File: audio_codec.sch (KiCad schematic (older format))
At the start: 11 parts

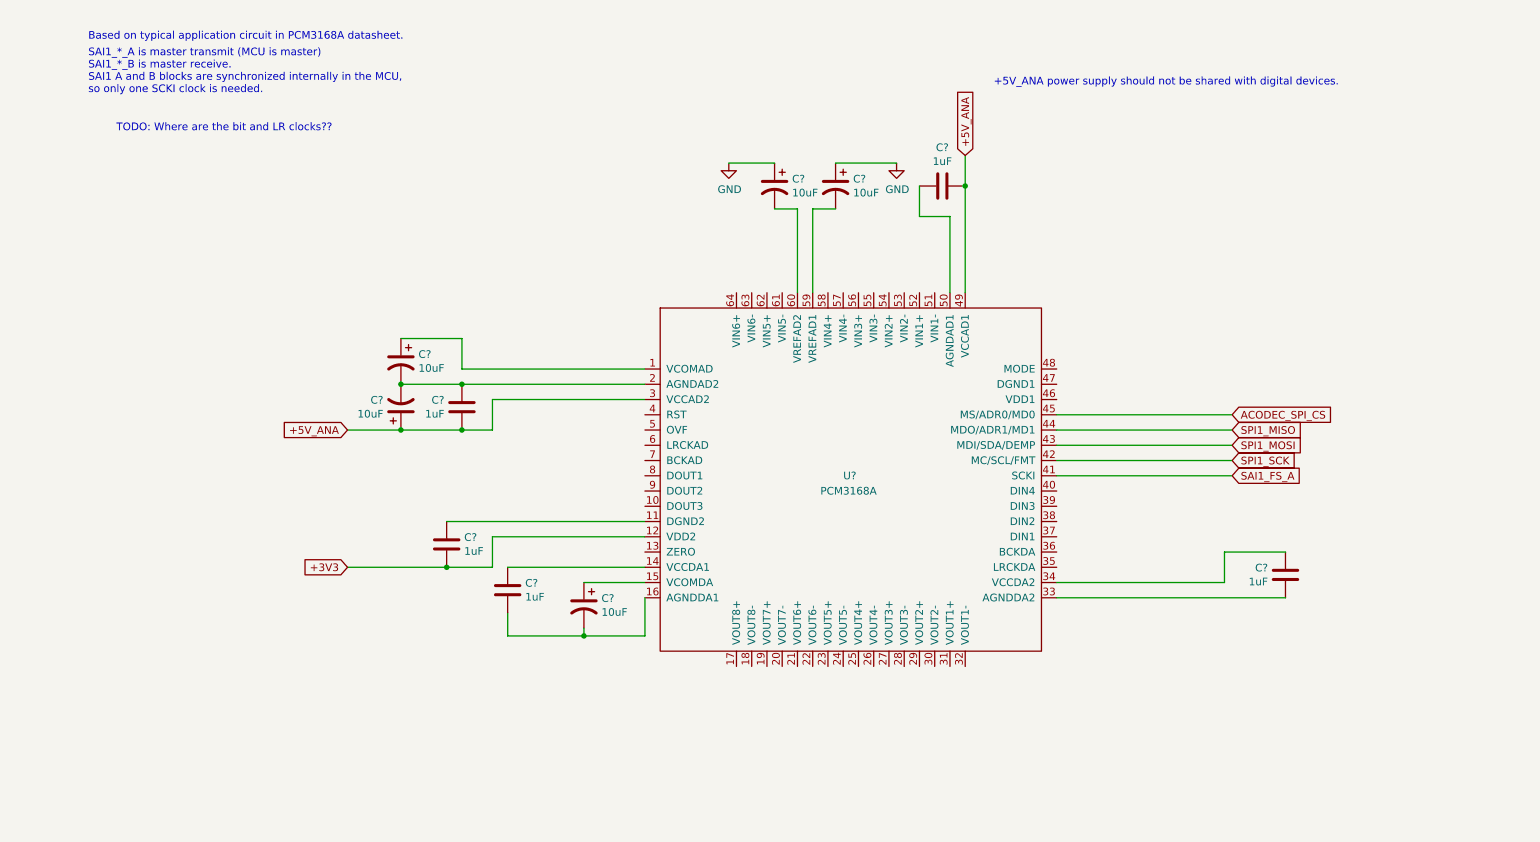
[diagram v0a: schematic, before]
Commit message: Finished digital part of CODEC
Needed to add SAI2 to get enough pins.
We could have multiplexed all 8 channels on one pin but the SR is limited to
48KHz. I wanted to see how it works with 2 data lines per direction. Then
maximum SR is 96KHz, which we probably won't use but at least its not at the
limit.
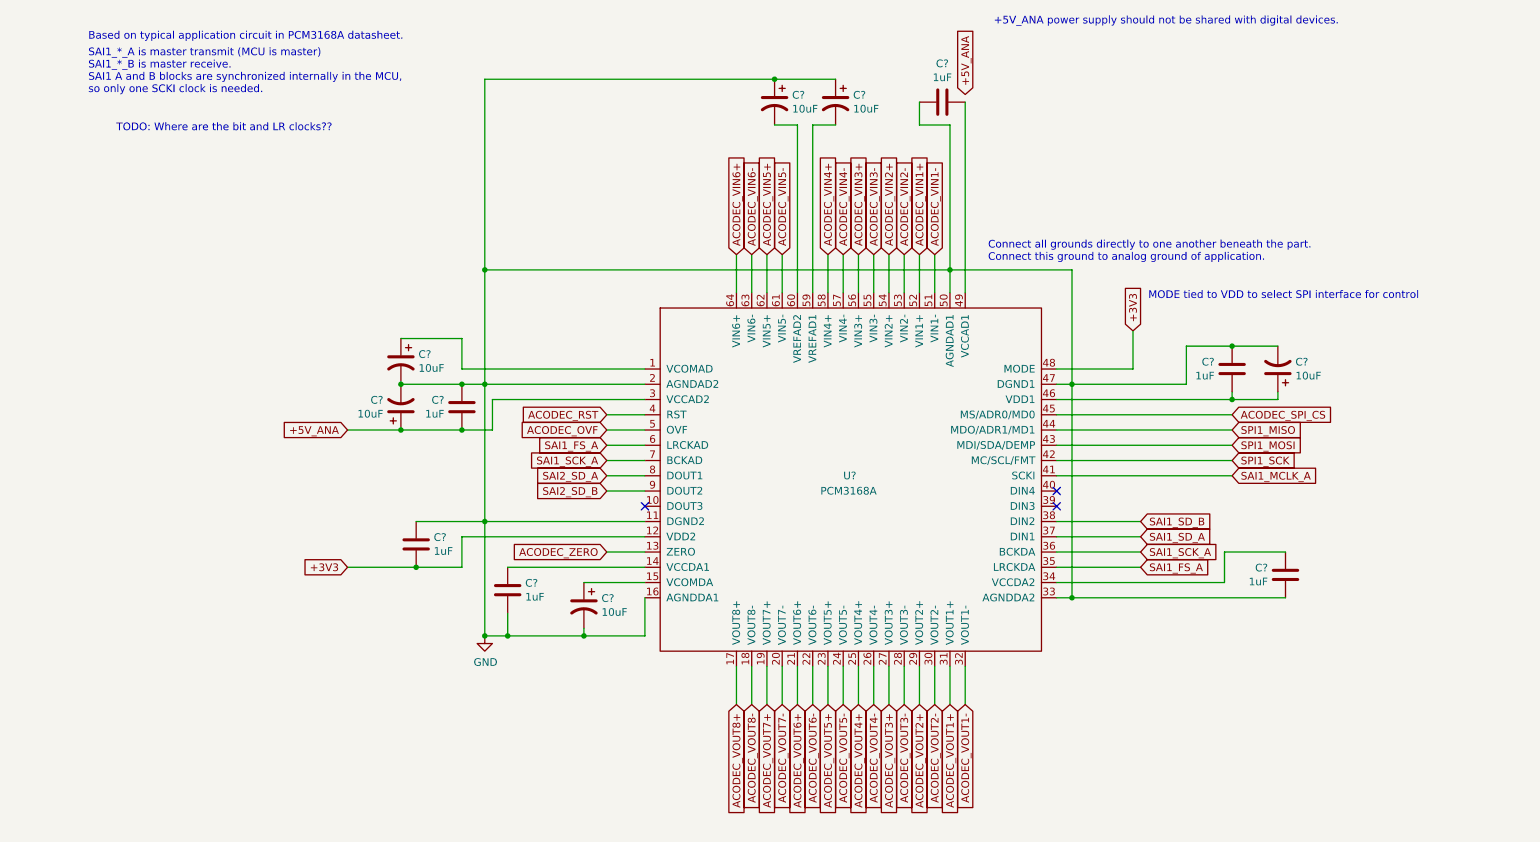
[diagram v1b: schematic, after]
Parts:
- added C?: 1uF, symbol Device:C
- added C?: 10uF, symbol Device:CP1
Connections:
- net +3V3: now also U?.48 (MODE)
- net +5V_ANA: no longer C?.1, U?.49 (VCCAD1)
- net GND: now also C?.1, C?.1, C?.2, C?.2, C?.2, C?.2, C?.2, C?.2, U?.11 (DGND2), U?.16 (AGNDDA1), U?.2 (AGNDAD2), U?.33 (AGNDDA2), U?.47 (DGND1), U?.50 (AGNDAD1), C?.1, C?.2
- net SAI1_FS_A: now also U?.35 (LRCKDA), U?.6 (LRCKAD); no longer U?.41 (SCKI)
- net ACODEC_ZERO: now reaches U?.13 (ZERO)
- net ACODEC_VOUT8+: now reaches U?.17 (VOUT8+)
- net ACODEC_VOUT8-: now reaches U?.18 (VOUT8-)
- net ACODEC_VOUT7+: now reaches U?.19 (VOUT7+)
- net ACODEC_VOUT7-: now reaches U?.20 (VOUT7-)
- net ACODEC_VOUT6+: now reaches U?.21 (VOUT6+)
- net ACODEC_VOUT6-: now reaches U?.22 (VOUT6-)
- net ACODEC_VOUT5+: now reaches U?.23 (VOUT5+)
- net ACODEC_VOUT5-: now reaches U?.24 (VOUT5-)
- net ACODEC_VOUT4+: now reaches U?.25 (VOUT4+)
- net ACODEC_VOUT4-: now reaches U?.26 (VOUT4-)
- net ACODEC_VOUT3+: now reaches U?.27 (VOUT3+)
- net ACODEC_VOUT3-: now reaches U?.28 (VOUT3-)
- net ACODEC_VOUT2+: now reaches U?.29 (VOUT2+)
- net ACODEC_VOUT2-: now reaches U?.30 (VOUT2-)
- net ACODEC_VOUT1+: now reaches U?.31 (VOUT1+)
- net ACODEC_VOUT1-: now reaches U?.32 (VOUT1-)
- net SAI1_SCK_A: now reaches U?.36 (BCKDA)
- net SAI1_SCK_A: now also U?.7 (BCKAD)
- net SAI1_SD_A: now reaches U?.37 (DIN1)
- net SAI1_SD_B: now reaches U?.38 (DIN2)
- net ACODEC_RST: now reaches U?.4 (RST)
- net at U?.46 (VDD1): now also C?.1, C?.2
- net ACODEC_OVF: now reaches U?.5 (OVF)
- net ACODEC_VIN1-: now reaches U?.51 (VIN1-)
- net ACODEC_VIN1+: now reaches U?.52 (VIN1+)
- net ACODEC_VIN2-: now reaches U?.53 (VIN2-)
- net ACODEC_VIN2+: now reaches U?.54 (VIN2+)
- net ACODEC_VIN3-: now reaches U?.55 (VIN3-)
- net ACODEC_VIN3+: now reaches U?.56 (VIN3+)
- net ACODEC_VIN4-: now reaches U?.57 (VIN4-)
- net ACODEC_VIN4+: now reaches U?.58 (VIN4+)
- net ACODEC_VIN5-: now reaches U?.61 (VIN5-)
- net ACODEC_VIN5+: now reaches U?.62 (VIN5+)
- net ACODEC_VIN6-: now reaches U?.63 (VIN6-)
- net ACODEC_VIN6+: now reaches U?.64 (VIN6+)
- net SAI2_SD_A: now reaches U?.8 (DOUT1)
- net SAI2_SD_B: now reaches U?.9 (DOUT2)
- new net: C?.1, U?.49 (VCCAD1)
- new net SAI1_MCLK_A: U?.41 (SCKI)
- no-connect marks 0 -> 3
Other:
- note added: "Connect all grounds directly to one another beneath the part.\nConnect this ground to analog ground of application."
- note added: "MODE tied to VDD to select SPI interface for control"
- moved on the sheet: C?

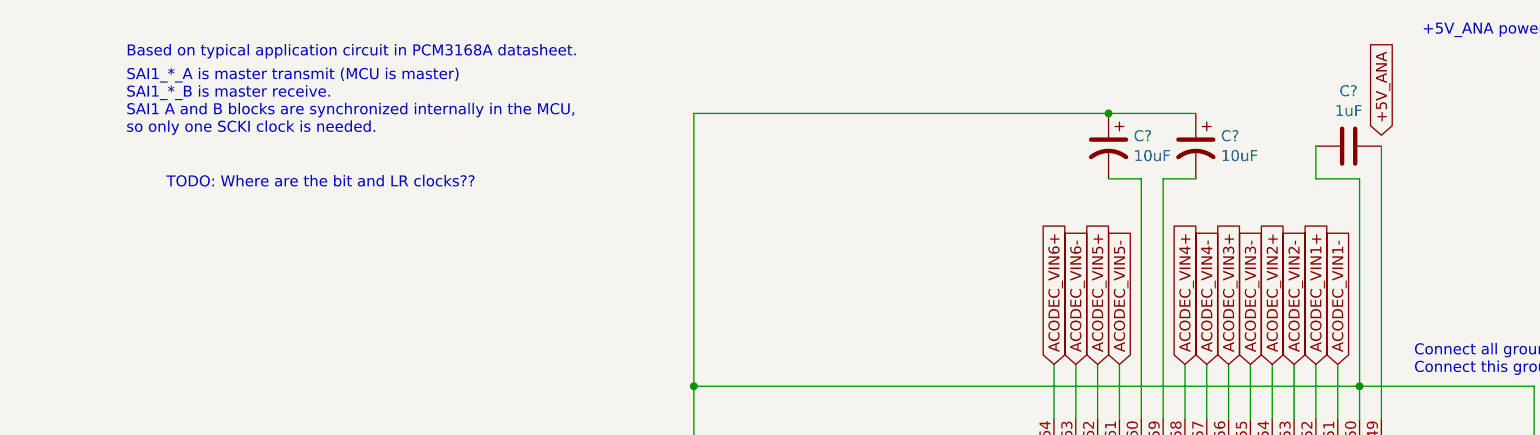
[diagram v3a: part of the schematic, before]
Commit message: Added MIDI
We will split the project into 2 boards:

A larger board will have jacks and extra pins, maybe the voltage regulators.

A smaller daughter card will have all the expensive small stuff: MCU, RAM, CODEC
etc. This also allows us to route differential signals to the MCU (this is
better than transmitting digital signals over long distances, with similar
fidelity, right?)
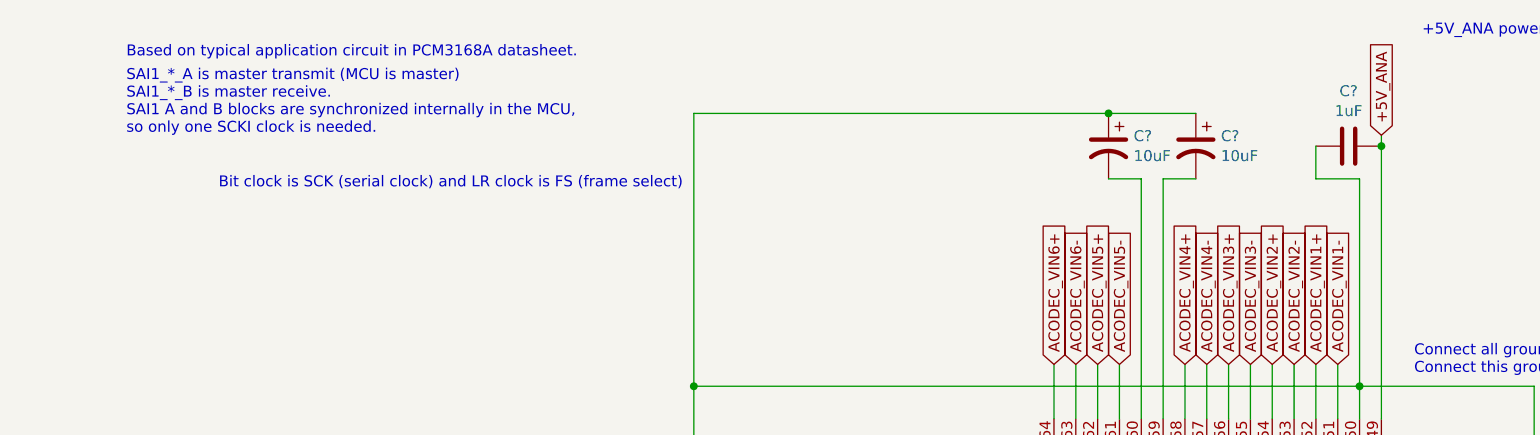
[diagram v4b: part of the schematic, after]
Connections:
- net +5V_ANA: now also C?.1, U?.49 (VCCAD1)
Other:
- note added: "Bit clock is SCK (serial clock) and LR clock is FS (frame select)"
- note removed: "TODO: Where are the bit and LR clocks??"
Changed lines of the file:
@@
 $Descr A4 11693 8268
 encoding utf-8
-Sheet 6 9
+Sheet 6 10
 Title ""
 Date ""
@@
 Wire Wire Line
 	8150 3550 7000 3550
-Text Notes 2250 1300 2    50   ~ 0
-TODO: Where are the bit and LR clocks??
+Text Notes 3200 1300 2    50   ~ 0
+Bit clock is SCK (serial clock) and LR clock is FS (frame select)
 Text GLabel 7500 2600 1    50   Input ~ 0
 +3V3
@@
 Wire Wire Line
 	4900 4800 4900 5050
+Wire Wire Line
+	6400 1050 6400 1100
+Connection ~ 6400 1100
 $EndSCHEMATC
